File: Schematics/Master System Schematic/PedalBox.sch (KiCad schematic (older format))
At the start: 4 parts, among them U1 CAN_Module

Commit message: Add CAN Bus Module to Pedal Box
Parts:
- removed U1: CAN_Module, symbol NER:CAN-Module
- added U?: CAN_Bus_Module, symbol NER:CAN_Bus_Module
- renumbered A1 to A?
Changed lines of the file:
@@
 $Descr A 11000 8500
 encoding utf-8
-Sheet 1 1
+Sheet 12 12
 Title "Pedal Box"
 Date "2020-09-20"
@@
 	3600 3050 4350 3050
 $Comp
-L NER:Arduino_UNO_rev3 A1
+L NER:Arduino_UNO_rev3 A?
 U 1 1 5F6833F8
 P 4950 2900
-F 0 "A1" H 4950 3015 50  0000 C CNN
+F 0 "A?" H 4950 3015 50  0000 C CNN
 F 1 "Arduino_UNO_rev3" H 4950 2924 50  0000 C CNN
 F 2 "" H 4950 3050 50  0001 C CNN
@@
 	1    0    0    -1
 $EndComp
-$Comp
-L NER:CAN-Module U1
-U 1 1 5F6A22C3
-P 7600 3100
-F 0 "U1" H 7625 3115 50  0000 C CNN
-F 1 "CAN_Module" H 7625 3024 50  0000 C CNN
-F 2 "" H 7600 3100 50  0001 C CNN
-F 3 "" H 7600 3100 50  0001 C CNN
-	1    7600 3100
-	1    0    0    -1
-$EndComp
 Wire Wire Line
 	7050 3450 5900 3450
@@
 Wire Wire Line
 	5750 3550 5550 3550
-Text HLabel 8950 3650 2    50   Input ~ 0
+Text HLabel 8950 3750 2    50   Input ~ 0
 CAN_L
 Text HLabel 8950 3500 2    50   Input ~ 0
@@
 	8200 3500 8950 3500
 Wire Wire Line
-	8950 3650 8200 3650
+	8950 3750 8200 3750
 NoConn ~ 4350 3200
 NoConn ~ 4350 3300
@@
 	6000 5650 6600 5650
 NoConn ~ 4350 4150
+$Comp
+L NER:CAN_Bus_Module U?
+U 1 1 5F6D982E
+P 7600 3200
+F 0 "U?" H 7625 3315 50  0000 C CNN
+F 1 "CAN_Bus_Module" H 7625 3224 50  0000 C CNN
+F 2 "" H 7600 3200 50  0001 C CNN
+F 3 "" H 7600 3200 50  0001 C CNN
+	1    7600 3200
+	1    0    0    -1
+$EndComp
 $EndSCHEMATC

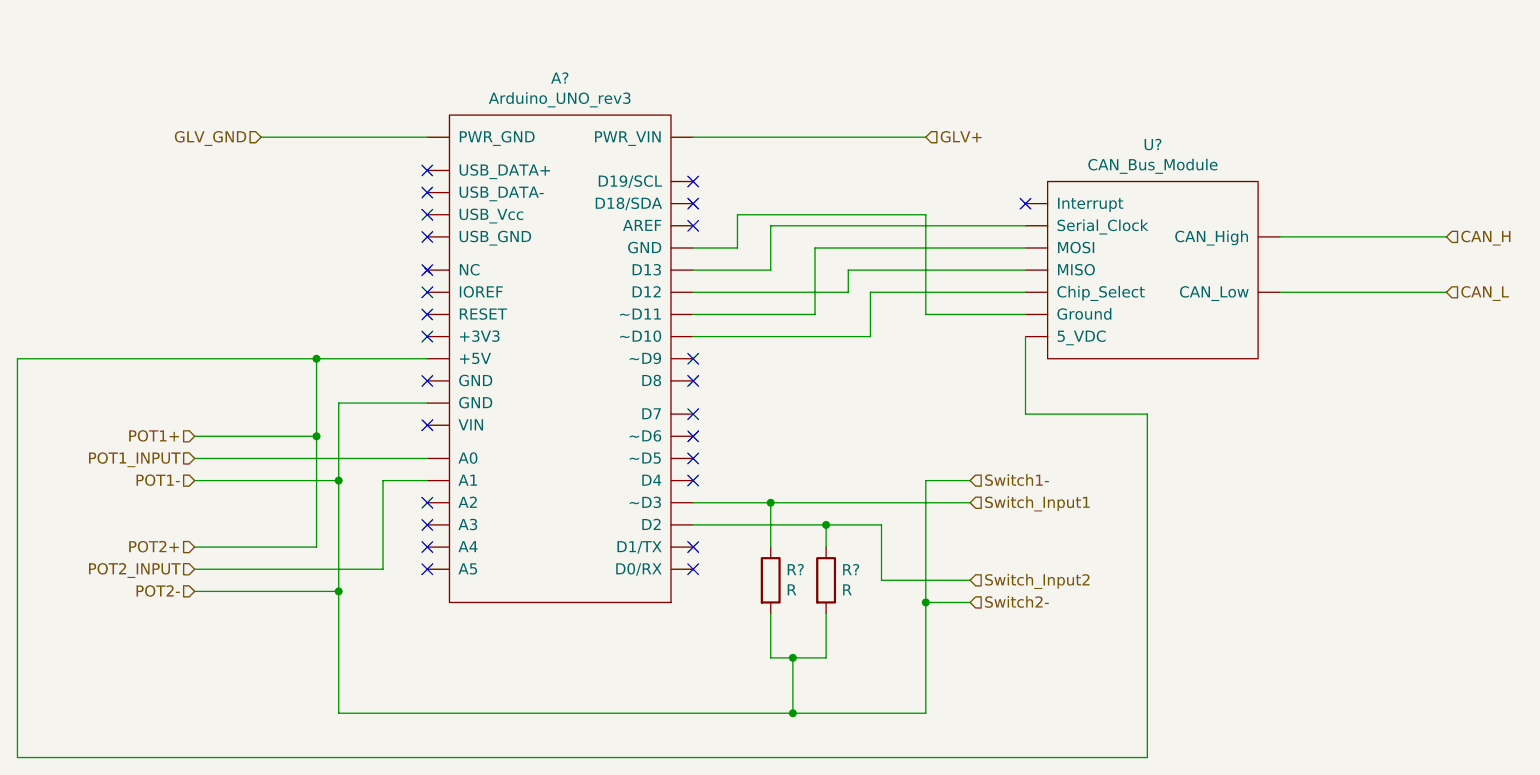
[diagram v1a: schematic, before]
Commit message: Connectors and Start of Numbering
Created new generic connectors and applied numbering tool to whole project
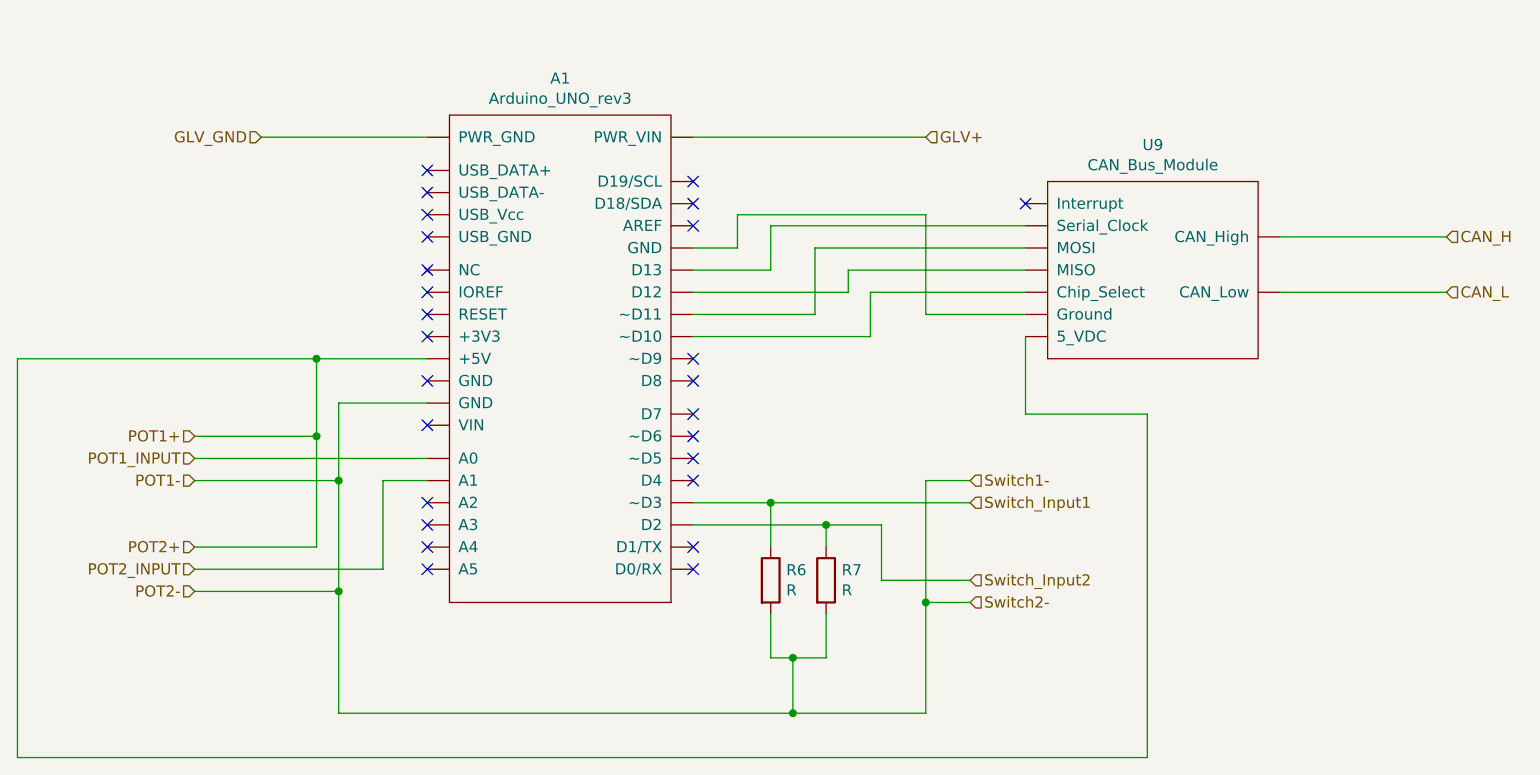
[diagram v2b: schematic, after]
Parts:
- gave numbers to parts that had none: 4
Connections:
- new net: A1.~ (~~D9), U9.~ (Serial_Clock) (x5)
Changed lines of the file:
@@
 EESchema Schematic File Version 4
+LIBS:Master System Schematic-cache
 EELAYER 30 0
 EELAYER END
@@
 	3600 3050 4350 3050
 $Comp
-L NER:Arduino_UNO_rev3 A?
+L NER:Arduino_UNO_rev3 A1
 U 1 1 5F6833F8
 P 4950 2900
-F 0 "A?" H 4950 3015 50  0000 C CNN
+F 0 "A1" H 4950 3015 50  0000 C CNN
 F 1 "Arduino_UNO_rev3" H 4950 2924 50  0000 C CNN
 F 2 "" H 4950 3050 50  0001 C CNN
@@
 Connection ~ 5900 4700
 $Comp
-L Device:R R?
+L Device:R R6
 U 1 1 5F71A5F5
 P 5900 5050
-F 0 "R?" H 5970 5096 50  0000 L CNN
+F 0 "R6" H 5970 5096 50  0000 L CNN
 F 1 "R" H 5970 5005 50  0000 L CNN
 F 2 "" V 5830 5050 50  0001 C CNN
@@
 $EndComp
 $Comp
-L Device:R R?
+L Device:R R7
 U 1 1 5F71A986
 P 6150 5050
-F 0 "R?" H 6220 5096 50  0000 L CNN
+F 0 "R7" H 6220 5096 50  0000 L CNN
 F 1 "R" H 6220 5005 50  0000 L CNN
 F 2 "" V 6080 5050 50  0001 C CNN
@@
 NoConn ~ 4350 4150
 $Comp
-L NER:CAN_Bus_Module U?
+L NER:CAN_Bus_Module U9
 U 1 1 5F6D982E
 P 7600 3200
-F 0 "U?" H 7625 3315 50  0000 C CNN
+F 0 "U9" H 7625 3315 50  0000 C CNN
 F 1 "CAN_Bus_Module" H 7625 3224 50  0000 C CNN
 F 2 "" H 7600 3200 50  0001 C CNN

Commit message: New Relay Module Symbol/ Some Parts Added to Driver IO Container
(Note: Make sure to check that I didn't make some catastrophically horrible changes to everything by accident)
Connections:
- new net: A1.~ (~~D9), U9.~ (Serial_Clock) (x5)
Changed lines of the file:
@@
 EESchema Schematic File Version 4
-LIBS:Master System Schematic-cache
 EELAYER 30 0
 EELAYER END

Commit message: Finished IO Container, Added Brake Light
In the IO Container: made connections between Speaker, Arduino, CAN, Relay Module, and Button. Made new symbol for the Button.

In Master Schematic: added Brake Light Container.

In Brake Light Container: made connections between CAN, Relay Module, and Arduino. Still missing LED (but that will be in Master Schematic.)
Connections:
- new net: A1.~ (~~D9), U9.~ (Serial_Clock) (x5)
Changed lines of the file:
@@
 $Descr A 11000 8500
 encoding utf-8
-Sheet 12 12
+Sheet 12 13
 Title "Pedal Box"
 Date "2020-09-20"

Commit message: Moved BMS Current Sensor
Moved current sensor to be inside the accumulator container, as it physically will be
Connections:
- new net: A1.~ (~~D9), U9.~ (Serial_Clock) (x5)
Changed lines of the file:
@@
 EESchema Schematic File Version 4
+LIBS:Master System Schematic-cache
 EELAYER 30 0
 EELAYER END
